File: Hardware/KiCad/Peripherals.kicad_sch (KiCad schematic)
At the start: 61 parts

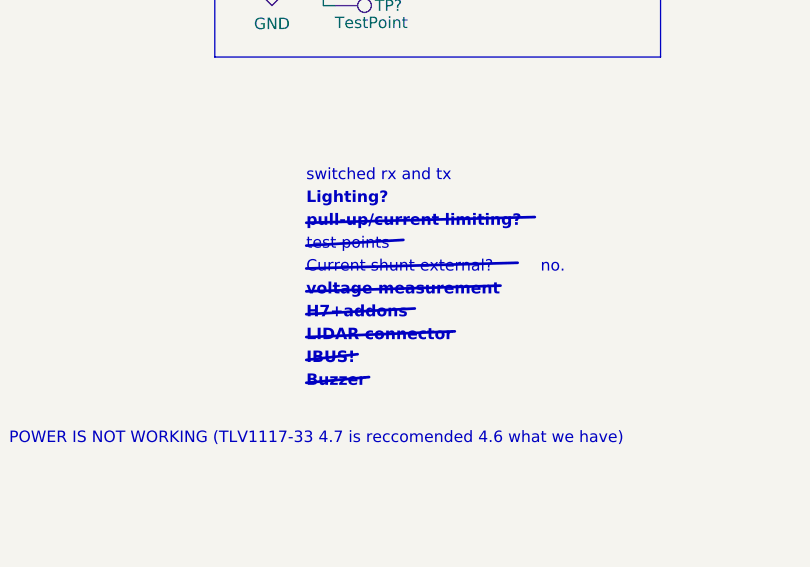
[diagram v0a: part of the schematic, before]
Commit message: added all footprints and reorganized schematic
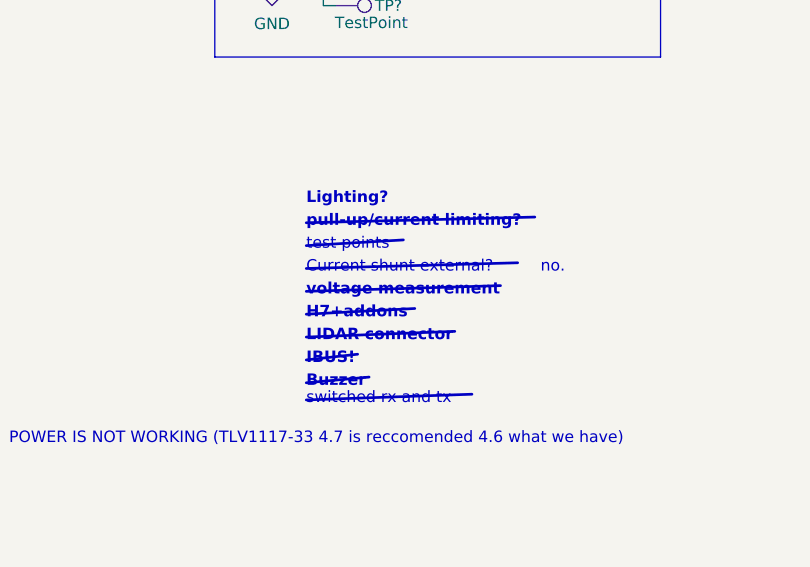
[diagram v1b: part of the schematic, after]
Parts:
- TP? (x14): footprint (none) -> TestPoint:TestPoint_Pad_D1.5mm
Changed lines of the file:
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@@
     (stroke (width 0) (type default) (color 0 0 0 0))
+  )
+  (polyline (pts (xy 234.95 159.385) (xy 253.365 158.75))
+    (stroke (width 0.3) (type solid) (color 0 0 0 0))
   )
   (wire (pts (xy 170.815 100.33) (xy 170.815 101.6))
@@
     (effects (font (size 1.27 1.27)) (justify left bottom))
   )
-  (text "switched rx and tx" (at 234.95 135.255 0)
+  (text "switched rx and tx" (at 234.95 160.02 0)
     (effects (font (size 1.27 1.27)) (justify left bottom))
   )
@@
       (effects (font (size 1.27 1.27)) (justify left))
     )
-    (property "Footprint" "" (id 2) (at 238.125 116.205 0)
+    (property "Footprint" "TestPoint:TestPoint_Pad_D1.5mm" (id 2) (at 238.125 116.205 0)
       (effects (font (size 1.27 1.27)) hide)
     )
@@
       (effects (font (size 1.27 1.27)) (justify left))
     )
-    (property "Footprint" "" (id 2) (at 238.125 106.045 0)
+    (property "Footprint" "TestPoint:TestPoint_Pad_D1.5mm" (id 2) (at 238.125 106.045 0)
       (effects (font (size 1.27 1.27)) hide)
     )
@@
       (effects (font (size 1.27 1.27)) (justify left))
     )
-    (property "Footprint" "" (id 2) (at 238.125 93.98 0)
+    (property "Footprint" "TestPoint:TestPoint_Pad_D1.5mm" (id 2) (at 238.125 93.98 0)
       (effects (font (size 1.27 1.27)) hide)
     )
@@
       (effects (font (size 1.27 1.27)) (justify left))
     )
-    (property "Footprint" "" (id 2) (at 238.125 98.425 0)
+    (property "Footprint" "TestPoint:TestPoint_Pad_D1.5mm" (id 2) (at 238.125 98.425 0)
       (effects (font (size 1.27 1.27)) hide)
     )
@@
       (effects (font (size 1.27 1.27)) (justify left))
     )
-    (property "Footprint" "" (id 2) (at 238.125 120.65 0)
+    (property "Footprint" "TestPoint:TestPoint_Pad_D1.5mm" (id 2) (at 238.125 120.65 0)
       (effects (font (size 1.27 1.27)) hide)
     )
@@
       (effects (font (size 1.27 1.27)) (justify left))
     )
-    (property "Footprint" "" (id 2) (at 262.89 102.87 0)
+    (property "Footprint" "TestPoint:TestPoint_Pad_D1.5mm" (id 2) (at 262.89 102.87 0)
       (effects (font (size 1.27 1.27)) hide)
     )
@@
       (effects (font (size 1.27 1.27)) (justify left))
     )
-    (property "Footprint" "" (id 2) (at 170.815 156.845 0)
+    (property "Footprint" "TestPoint:TestPoint_Pad_D1.5mm" (id 2) (at 170.815 156.845 0)
       (effects (font (size 1.27 1.27)) hide)
     )
@@
       (effects (font (size 1.27 1.27)) (justify left))
     )
-    (property "Footprint" "" (id 2) (at 170.815 152.4 0)
+    (property "Footprint" "TestPoint:TestPoint_Pad_D1.5mm" (id 2) (at 170.815 152.4 0)
       (effects (font (size 1.27 1.27)) hide)
     )
@@
       (effects (font (size 1.27 1.27)) (justify left))
     )
-    (property "Footprint" "" (id 2) (at 262.89 113.665 0)
+    (property "Footprint" "TestPoint:TestPoint_Pad_D1.5mm" (id 2) (at 262.89 113.665 0)
       (effects (font (size 1.27 1.27)) hide)
     )
@@
       (effects (font (size 1.27 1.27)) (justify left))
     )
-    (property "Footprint" "" (id 2) (at 238.125 110.49 0)
+    (property "Footprint" "TestPoint:TestPoint_Pad_D1.5mm" (id 2) (at 238.125 110.49 0)
       (effects (font (size 1.27 1.27)) hide)
     )
@@
       (effects (font (size 1.27 1.27)) (justify left))
     )
-    (property "Footprint" "" (id 2) (at 262.89 98.425 0)
+    (property "Footprint" "TestPoint:TestPoint_Pad_D1.5mm" (id 2) (at 262.89 98.425 0)
       (effects (font (size 1.27 1.27)) hide)
     )
@@
       (effects (font (size 1.27 1.27)) (justify left))
     )
-    (property "Footprint" "" (id 2) (at 262.89 109.22 0)
+    (property "Footprint" "TestPoint:TestPoint_Pad_D1.5mm" (id 2) (at 262.89 109.22 0)
       (effects (font (size 1.27 1.27)) hide)
     )
@@
       (effects (font (size 1.27 1.27)) (justify left))
     )
-    (property "Footprint" "" (id 2) (at 170.815 147.955 0)
+    (property "Footprint" "TestPoint:TestPoint_Pad_D1.5mm" (id 2) (at 170.815 147.955 0)
       (effects (font (size 1.27 1.27)) hide)
     )
@@
       (effects (font (size 1.27 1.27)) (justify left))
     )
-    (property "Footprint" "" (id 2) (at 262.89 93.98 0)
-      (effects (font (size 1.27 1.27)) hide)
-    )
+    (property "Footprint" "TestPoint:TestPoint_Pad_D1.5mm" (id 2) (at 262.89 93.98 0)
+      (effects (font (size 1.27 1.27)) hide)
+    )

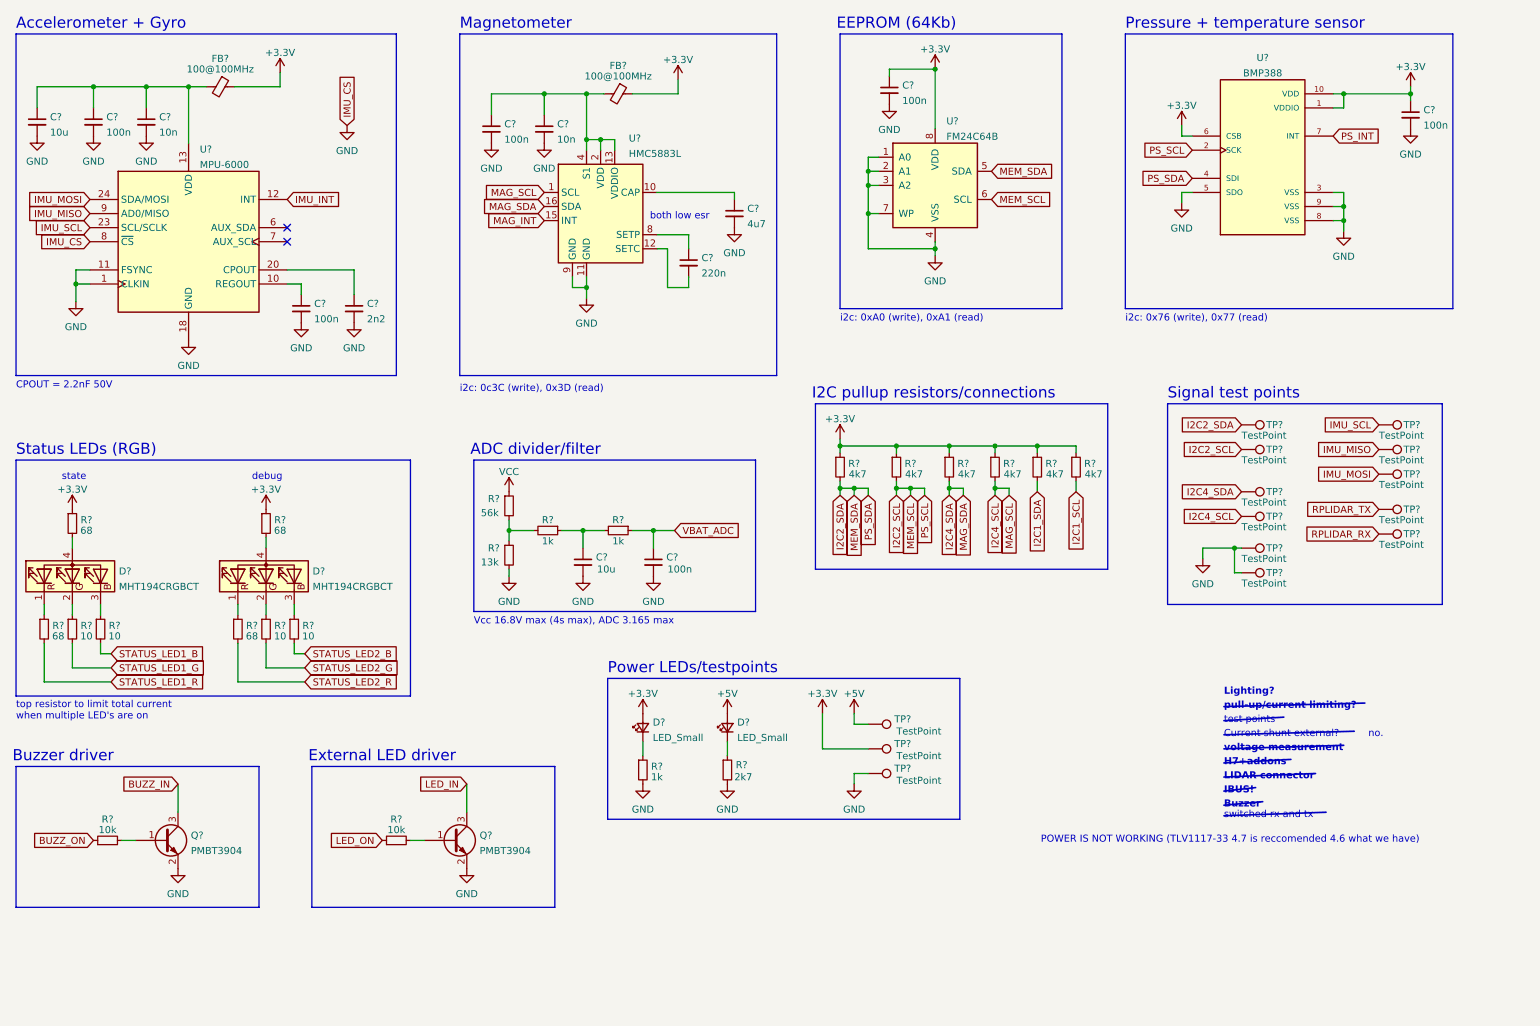
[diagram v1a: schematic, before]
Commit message: Fixed pullup being a pulldown for SDIO CD, added SD test points
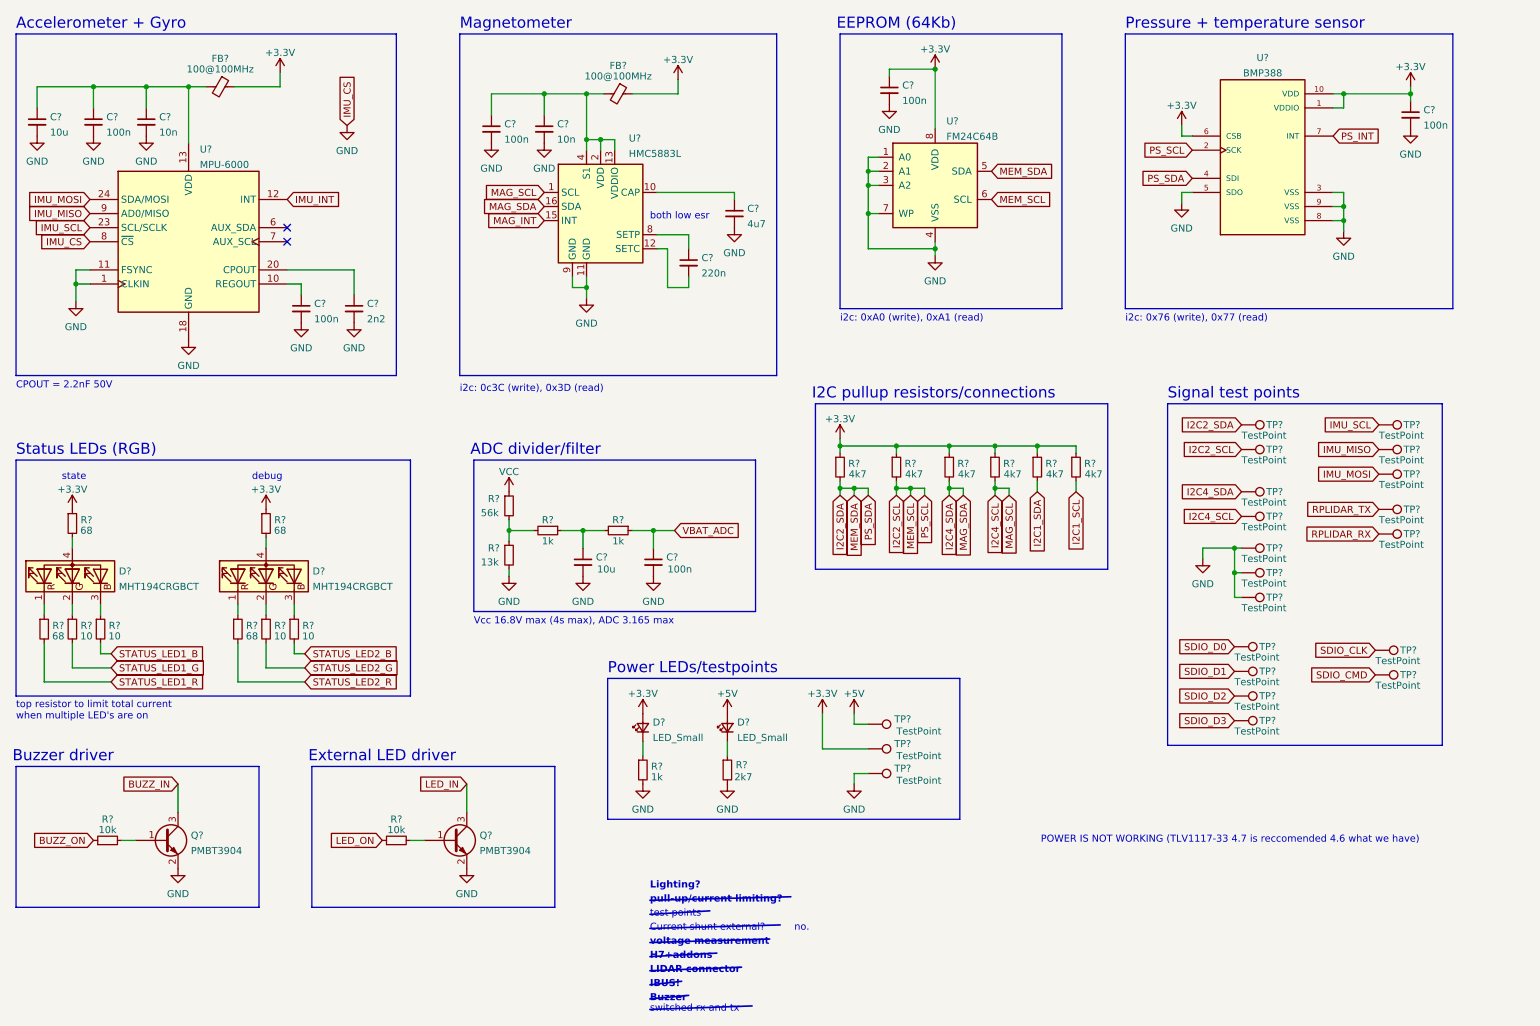
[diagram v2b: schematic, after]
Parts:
- added TP? (x7): TestPoint, TestPoint:TestPoint_Pad_D1.5mm, symbol Connector:TestPoint
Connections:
- net GND: now also TP?.1
- new net SDIO_CLK: TP?.1
- new net SDIO_CMD: TP?.1
- new net SDIO_D0: TP?.1
- new net SDIO_D1: TP?.1
- new net SDIO_D2: TP?.1
- new net SDIO_D3: TP?.1

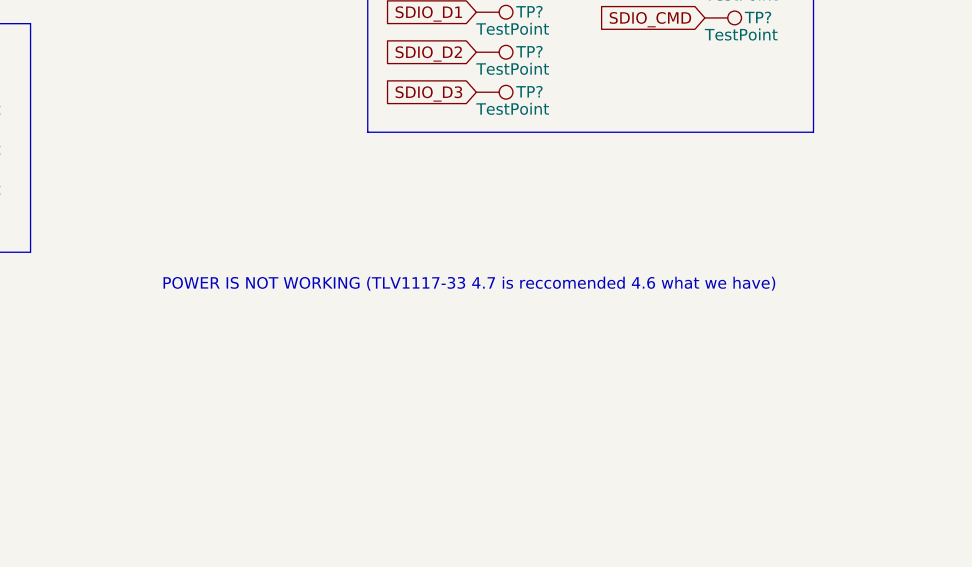
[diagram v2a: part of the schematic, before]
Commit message: Added a missing connection between the BECs and the LDO, removed some duplicate ferrite bead filtering
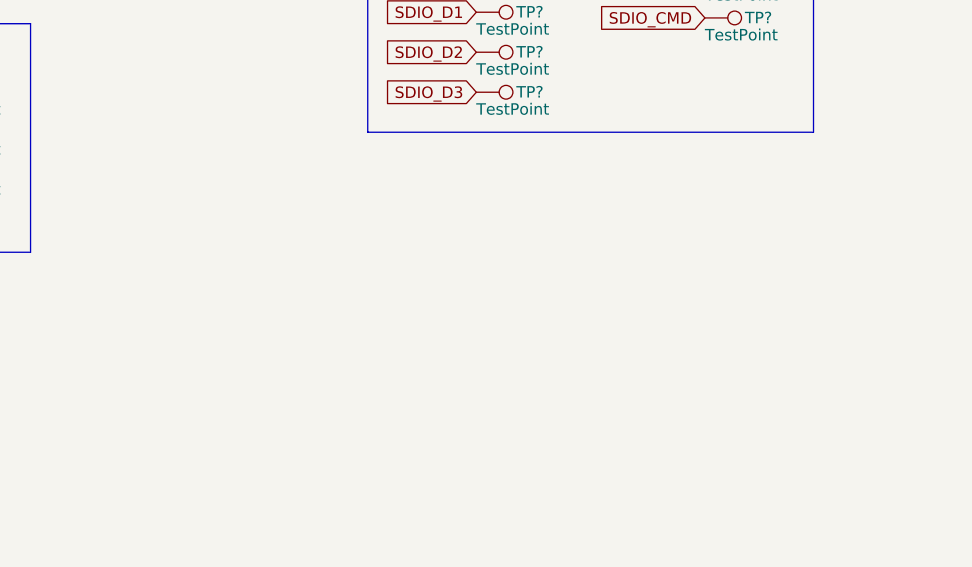
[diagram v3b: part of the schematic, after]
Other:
- note removed: "POWER IS NOT WORKING (TLV1117-33 4.7 is reccomended 4.6 what we have)"
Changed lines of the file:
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@@
     (effects (font (size 1.27 1.27) (thickness 0.254) bold) (justify left bottom))
-  )
-  (text "POWER IS NOT WORKING (TLV1117-33 4.7 is reccomended 4.6 what we have)"
-    (at 201.93 164.465 0)
-    (effects (font (size 1.27 1.27)) (justify left bottom))
   )
   (text "i2c: 0x76 (write), 0x77 (read)" (at 217.17 70.485 0)

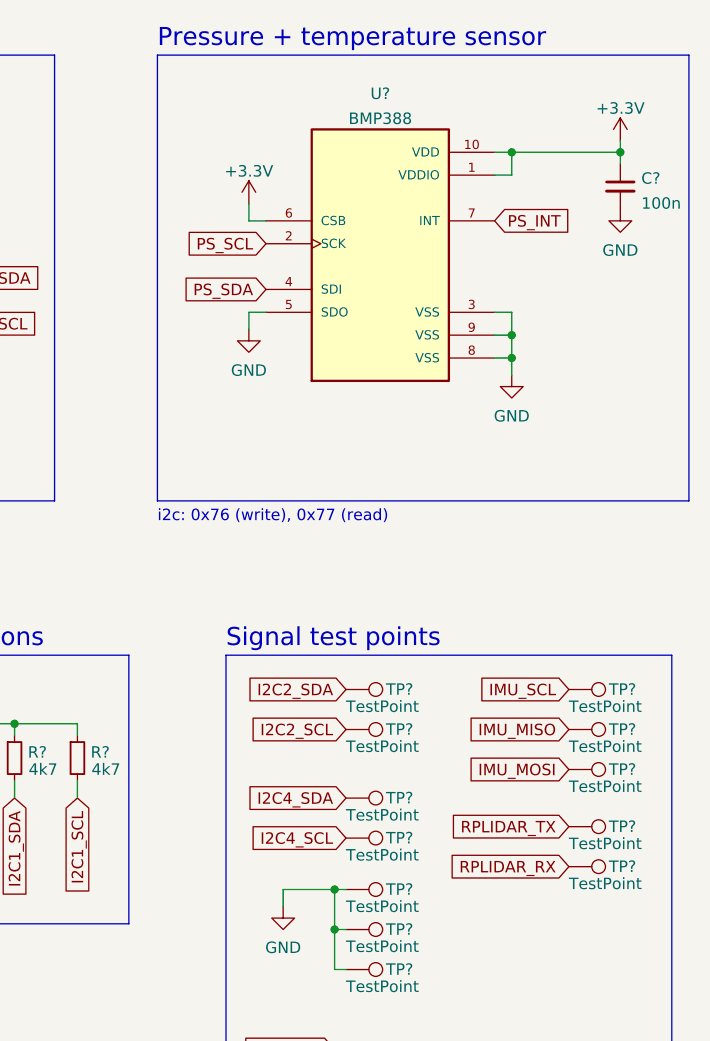
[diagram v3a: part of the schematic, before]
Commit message: Added more filtering for the BMP, small labeling changes
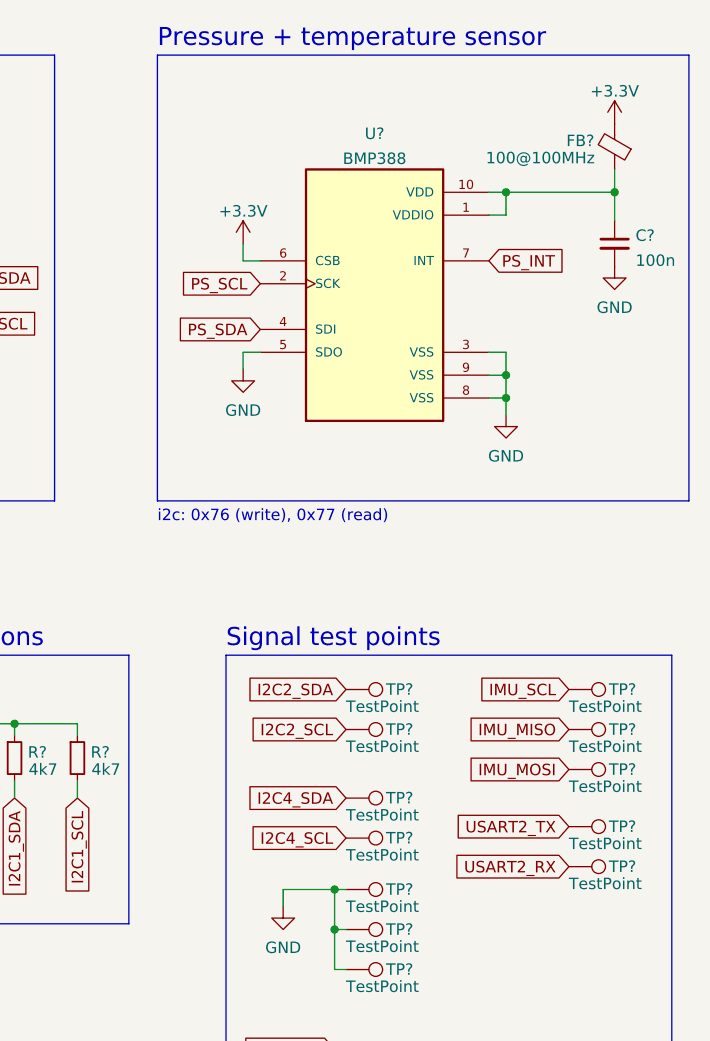
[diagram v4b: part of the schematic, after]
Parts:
- added FB?: 100@100MHz, Inductor_SMD:L_0603_1608Metric, symbol Device:FerriteBead_Small
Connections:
- net +3V3: now also FB?.2; no longer C?.1, U?.1 (VDDIO), U?.10 (VDD)
- net RPLIDAR_RX renamed USART2_RX
- net RPLIDAR_TX renamed USART2_TX
- new net: C?.1, FB?.1, U?.1 (VDDIO), U?.10 (VDD)
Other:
- moved on the sheet: C?, U?
